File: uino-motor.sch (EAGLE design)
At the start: 26 parts, among them IC1 TB6612FNG, J1 CON_TERMINAL_BLOCK_02-5MM, J2 CON_TERMINAL_BLOCK_02-5MM, J3 CON_TERMINAL_BLOCK_02-5MM, Q1 P-FET, U1 74*1G57, U2 74*1G57

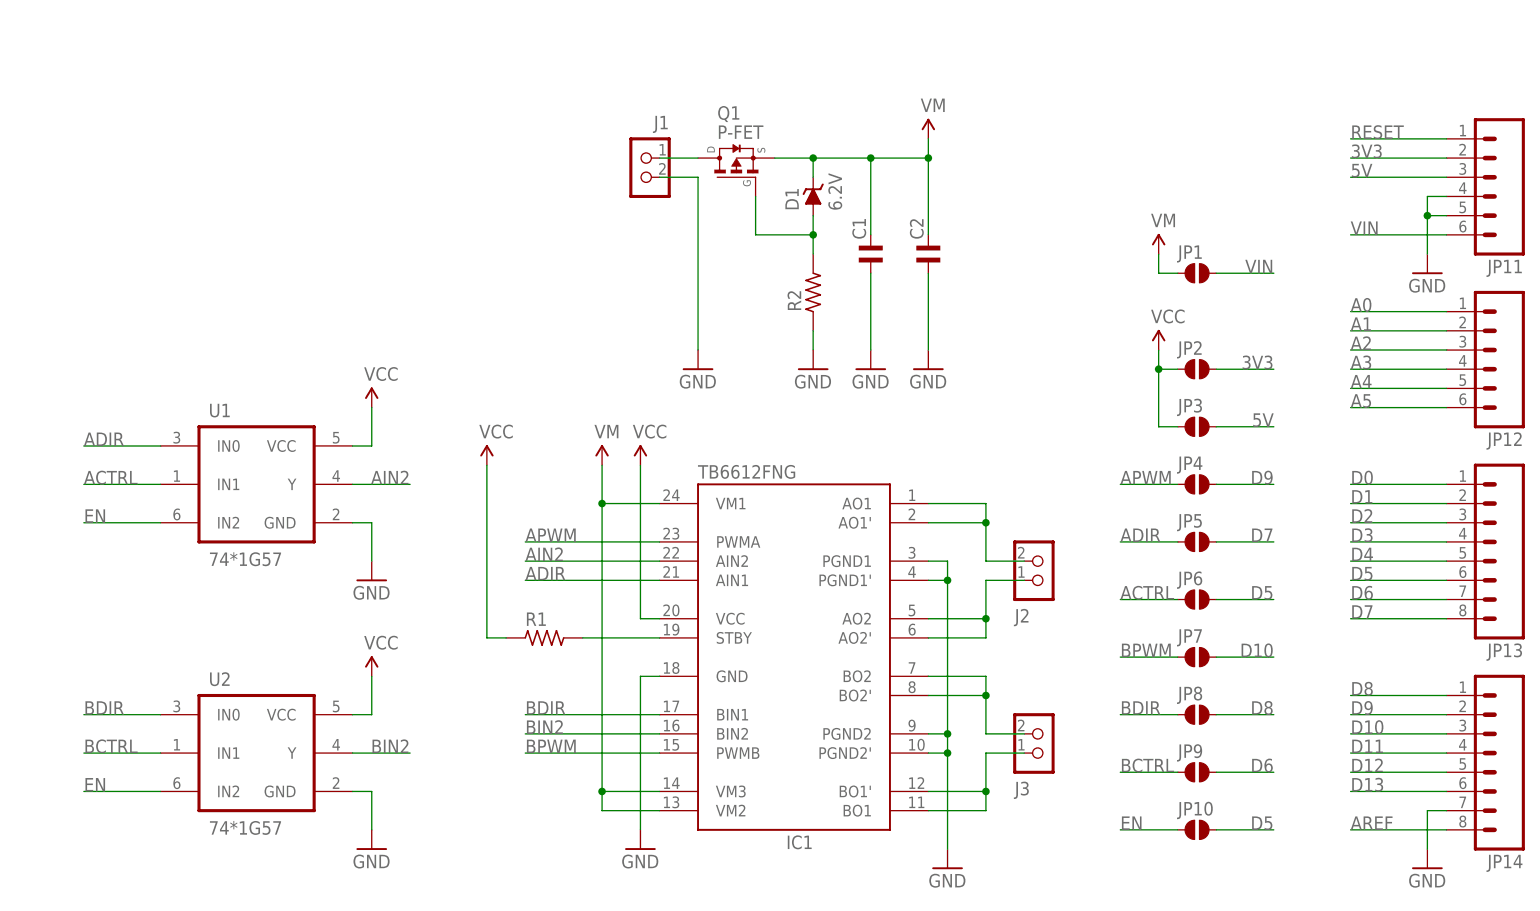
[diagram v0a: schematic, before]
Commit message: Added pull-down at logic gate inputs.  Routed board.
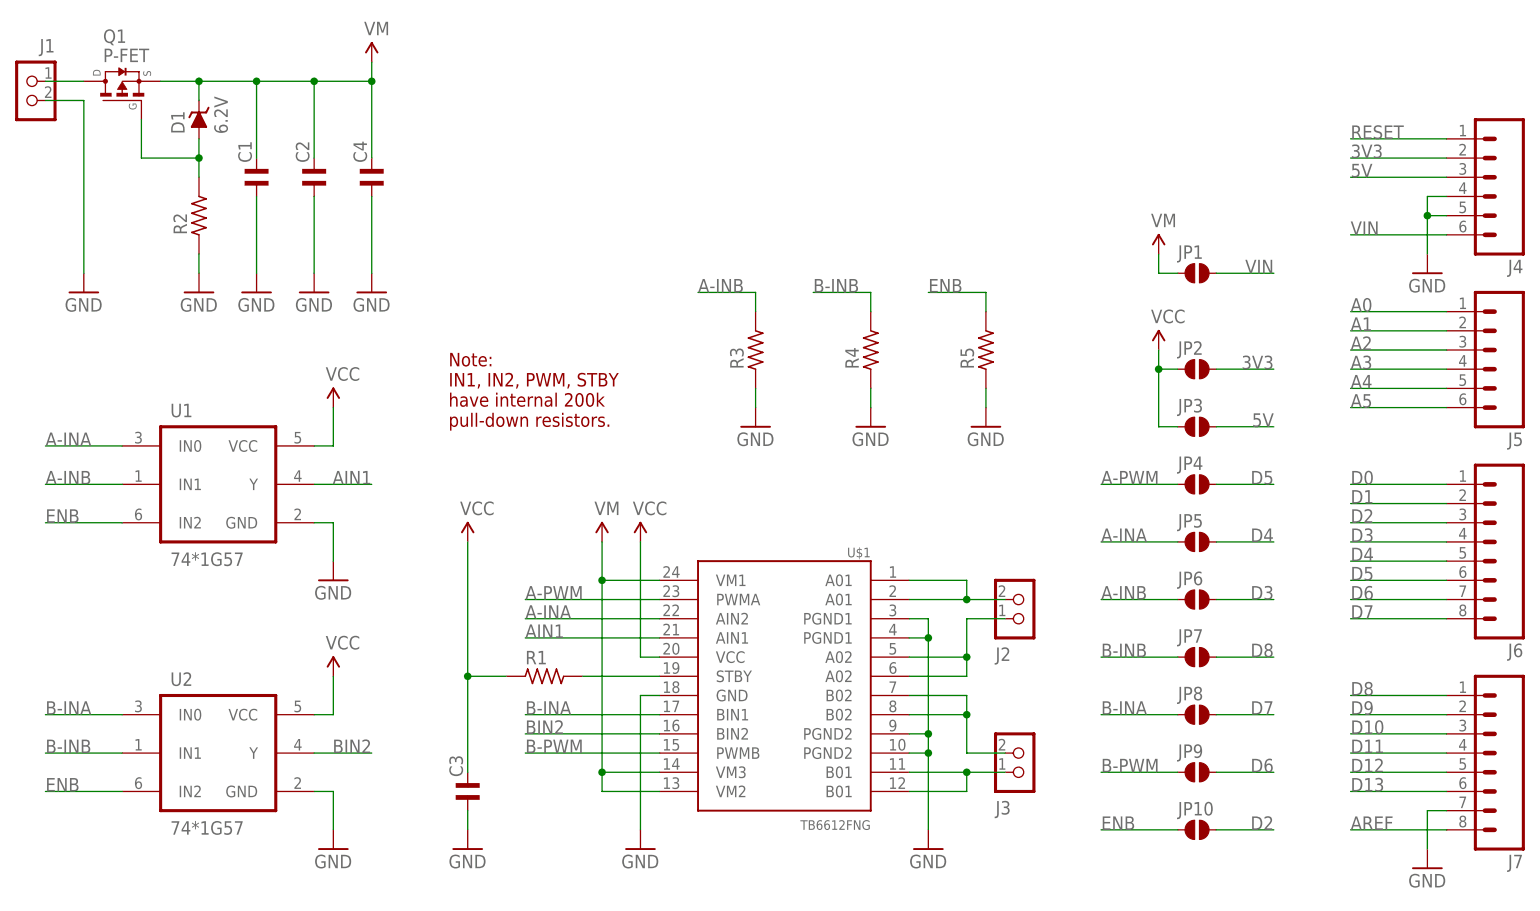
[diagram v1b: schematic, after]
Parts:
- removed IC1: TB6612FNG, adafruit:TB6612FNG
- added C3, C4: (no value), rc-master-smd:C_0805MP
- added R3, R4, R5: (no value), rc-master-smd:R_0805MP
- added U$1: TB6612FNG, SparkFun-PowerIC:TB6612FNG
- JP1, JP10, JP2, JP3, JP4, JP5, JP6, JP7, JP8, JP9: value SJ-055 -> SJ-035; device jumpers:SJ-055 -> jumpers:SJ-035
- renumbered JP11 to J4, JP12 to J5, JP13 to J6, JP14 to J7
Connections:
- removed net ACTRL: JP6.1, U1.IN1
- removed net ADIR: IC1.AIN1, JP5.1, U1.IN0
- removed net AIN2: IC1.AIN2, U1.Y
- removed net APWM: IC1.PWMA, JP4.1
- removed net BCTRL: JP9.1, U2.IN1
- removed net BDIR: IC1.BIN1, JP8.1, U2.IN0
- removed net BPWM: IC1.PWMB, JP7.1
- removed net EN: JP10.1, U1.IN2, U2.IN2
- removed net N$2: IC1.AO2, IC1.AO2', J2.1
- removed net N$3: IC1.BO2, IC1.BO2', J3.2
- removed net N$4: IC1.BO1, IC1.BO1', J3.1
- removed net N$5: IC1.STBY, R1.2
- new net A-INA: JP5.1, U$1.AIN2, U1.IN0
- new net A-INB: JP6.1, R3.2, U1.IN1
- new net A-PWM: JP4.1, U$1.PWMA
- new net AIN1: U$1.AIN1, U1.Y
- new net B-INA: JP8.1, U$1.BIN1, U2.IN0
- new net B-INB: JP7.1, R4.2, U2.IN1
- new net B-PWM: JP9.1, U$1.PWMB
- new net ENB: JP10.1, R5.2, U1.IN2, U2.IN2
- new net N$10: J2.2, U$1.A01@1, U$1.A01@2
- new net N$11: J3.1, U$1.B01@11, U$1.B01@12
- new net N$12: J2.1, U$1.A02@5, U$1.A02@6
- new net N$13: J3.2, U$1.B02@7, U$1.B02@8
- net BIN2: now also U$1.BIN2; no longer IC1.BIN2
- net D10: no longer JP7.2
- net D2: now also JP10.2
- net D3: now also JP6.2
- net D4: now also JP5.2
- net D5: now also JP4.2; no longer JP10.2, JP6.2
- net D7: now also JP8.2; no longer JP5.2
- net D8: now also JP7.2; no longer JP8.2
- net D9: no longer JP4.2
- net GND: now also C3.1, C4.1, R3.1, R4.1, R5.1, U$1.GND, U$1.PGND1@3, U$1.PGND1@4, U$1.PGND2@10, U$1.PGND2@9; no longer IC1.GND, IC1.PGND1, IC1.PGND1', IC1.PGND2, IC1.PGND2'
- net N$1: now also R1.2, U$1.STBY; no longer IC1.AO1, IC1.AO1', J2.2
- net VCC: now also C3.2, U$1.VCC; no longer IC1.VCC
- net VDD: now also C4.2, U$1.VM1, U$1.VM2, U$1.VM3; no longer IC1.VM1, IC1.VM2, IC1.VM3
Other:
- note added: "Note: IN1, IN2, PWM, STBY have internal 200k pull-down resistors."
- moved on the sheet: C1, C2, D1, J1, J2, J3, Q1, R1, R2, U1, U2

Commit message: Parts placed and major routing completed.
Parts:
- added F1: (no value), adi-misc:FUSE_PTC-TH
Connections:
- net N$10 renamed A01
- net N$11 renamed B01
- net N$12 renamed A02
- net N$13 renamed B02
- removed net N$8: J1.1, Q1.D
- new net N$5: F1.1, J1.1
- new net N$7: F1.2, Q1.D
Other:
- moved on the sheet: C1, C2, C4, D1, J1, Q1, R2
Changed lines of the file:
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@@
 <part name="R5" library="rc-master-smd" deviceset="R_" device="0805MP"/>
 <part name="GND15" library="SparkFun-Aesthetics" deviceset="GND" device=""/>
+<part name="F1" library="adi-misc" deviceset="FUSE_PTC" device="-TH"/>
 </parts>
 <sheets>
@@
 <instance part="J2" gate="CON" x="132.08" y="81.28" rot="MR180"/>
 <instance part="J3" gate="CON" x="132.08" y="60.96" rot="MR180"/>
-<instance part="J1" gate="CON" x="5.08" y="152.4" rot="MR0"/>
+<instance part="J1" gate="CON" x="12.7" y="134.62" rot="MR0"/>
 <instance part="GND8" gate="1" x="121.92" y="50.8"/>
 <instance part="GND3" gate="1" x="83.82" y="50.8"/>
@@
 <instance part="R1" gate="G$1" x="71.12" y="73.66"/>
 <instance part="SUPPLY3" gate="G$1" x="60.96" y="91.44"/>
-<instance part="Q1" gate="G$1" x="15.24" y="152.4" smashed="yes" rot="R90">
-<attribute name="VALUE" x="12.7" y="154.94" size="1.778" layer="96"/>
-<attribute name="NAME" x="12.7" y="157.48" size="1.778" layer="95"/>
+<instance part="Q1" gate="G$1" x="25.4" y="152.4" smashed="yes" rot="R90">
+<attribute name="VALUE" x="22.86" y="154.94" size="1.778" layer="96"/>
+<attribute name="NAME" x="22.86" y="157.48" size="1.778" layer="95"/>
 </instance>
-<instance part="D1" gate="G$1" x="25.4" y="147.32" rot="R90"/>
-<instance part="R2" gate="G$1" x="25.4" y="134.62" rot="R90"/>
-<instance part="GND5" gate="1" x="25.4" y="124.46"/>
-<instance part="SUPPLY6" gate="VDD" x="48.26" y="154.94"/>
-<instance part="C1" gate="G$1" x="33.02" y="139.7" rot="R90"/>
-<instance part="C2" gate="G$1" x="40.64" y="139.7" rot="R90"/>
-<instance part="GND6" gate="1" x="33.02" y="124.46"/>
-<instance part="GND7" gate="1" x="40.64" y="124.46"/>
-<instance part="GND4" gate="1" x="10.16" y="124.46"/>
+<instance part="D1" gate="G$1" x="35.56" y="147.32" rot="R90"/>
+<instance part="R2" gate="G$1" x="35.56" y="134.62" rot="R90"/>
+<instance part="GND5" gate="1" x="35.56" y="124.46"/>
+<instance part="SUPPLY6" gate="VDD" x="58.42" y="154.94"/>
+<instance part="C1" gate="G$1" x="43.18" y="139.7" rot="R90"/>
+<instance part="C2" gate="G$1" x="50.8" y="139.7" rot="R90"/>
+<instance part="GND6" gate="1" x="43.18" y="124.46"/>
+<instance part="GND7" gate="1" x="50.8" y="124.46"/>
+<instance part="GND4" gate="1" x="17.78" y="124.46"/>
 <instance part="JP2" gate="G$1" x="157.48" y="114.3"/>
 <instance part="JP3" gate="G$1" x="157.48" y="106.68"/>
@@
 <instance part="GND11" gate="1" x="60.96" y="50.8"/>
 <instance part="U$1" gate="G$1" x="101.6" y="73.66" rot="MR0"/>
-<instance part="C4" gate="G$1" x="48.26" y="139.7" rot="R90"/>
-<instance part="GND12" gate="1" x="48.26" y="124.46"/>
+<instance part="C4" gate="G$1" x="58.42" y="139.7" rot="R90"/>
+<instance part="GND12" gate="1" x="58.42" y="124.46"/>
 <instance part="R3" gate="G$1" x="99.06" y="116.84" rot="R90"/>
 <instance part="GND13" gate="1" x="99.06" y="106.68"/>
@@
 <instance part="R5" gate="G$1" x="129.54" y="116.84" rot="R90"/>
 <instance part="GND15" gate="1" x="129.54" y="106.68"/>
+<instance part="F1" gate="G$1" x="20.32" y="144.78" rot="R90"/>
 </instances>
 <busses>
@@
 <pinref part="C2" gate="G$1" pin="1"/>
 <pinref part="GND7" gate="1" pin="GND"/>
-<wire x1="40.64" y1="137.16" x2="40.64" y2="127" width="0.1524" layer="91"/>
+<wire x1="50.8" y1="137.16" x2="50.8" y2="127" width="0.1524" layer="91"/>
 </segment>
 <segment>
 <pinref part="C1" gate="G$1" pin="1"/>
 <pinref part="GND6" gate="1" pin="GND"/>
-<wire x1="33.02" y1="137.16" x2="33.02" y2="127" width="0.1524" layer="91"/>
-</segment>
-<segment>
-<pinref part="J1" gate="CON" pin="2"/>
-<pinref part="GND4" gate="1" pin="GND"/>
-<wire x1="5.08" y1="149.86" x2="10.16" y2="149.86" width="0.1524" layer="91"/>
-<wire x1="10.16" y1="149.86" x2="10.16" y2="127" width="0.1524" layer="91"/>
+<wire x1="43.18" y1="137.16" x2="43.18" y2="127" width="0.1524" layer="91"/>
 </segment>
 <segment>
 <pinref part="R2" gate="G$1" pin="1"/>
 <pinref part="GND5" gate="1" pin="GND"/>
-<wire x1="25.4" y1="129.54" x2="25.4" y2="127" width="0.1524" layer="91"/>
+<wire x1="35.56" y1="129.54" x2="35.56" y2="127" width="0.1524" layer="91"/>
 </segment>
 <segment>
@@
 <pinref part="C4" gate="G$1" pin="1"/>
 <pinref part="GND12" gate="1" pin="GND"/>
-<wire x1="48.26" y1="137.16" x2="48.26" y2="127" width="0.1524" layer="91"/>
+<wire x1="58.42" y1="137.16" x2="58.42" y2="127" width="0.1524" layer="91"/>
 </segment>
 <segment>
@@
 <pinref part="GND15" gate="1" pin="GND"/>
 <wire x1="129.54" y1="111.76" x2="129.54" y2="109.22" width="0.1524" layer="91"/>
+</segment>
+<segment>
+<pinref part="J1" gate="CON" pin="2"/>
+<pinref part="GND4" gate="1" pin="GND"/>
+<wire x1="12.7" y1="132.08" x2="17.78" y2="132.08" width="0.1524" layer="91"/>
+<wire x1="17.78" y1="132.08" x2="17.78" y2="127" width="0.1524" layer="91"/>
 </segment>
 </net>
@@
 <pinref part="C2" gate="G$1" pin="2"/>
 <pinref part="Q1" gate="G$1" pin="S"/>
-<wire x1="40.64" y1="152.4" x2="40.64" y2="142.24" width="0.1524" layer="91"/>
-<wire x1="20.32" y1="152.4" x2="25.4" y2="152.4" width="0.1524" layer="91"/>
-<junction x="40.64" y="152.4"/>
+<wire x1="50.8" y1="152.4" x2="50.8" y2="142.24" width="0.1524" layer="91"/>
+<wire x1="30.48" y1="152.4" x2="35.56" y2="152.4" width="0.1524" layer="91"/>
+<junction x="50.8" y="152.4"/>
 <pinref part="D1" gate="G$1" pin="C"/>
-<wire x1="25.4" y1="152.4" x2="33.02" y2="152.4" width="0.1524" layer="91"/>
-<wire x1="33.02" y1="152.4" x2="40.64" y2="152.4" width="0.1524" layer="91"/>
-<wire x1="25.4" y1="149.86" x2="25.4" y2="152.4" width="0.1524" layer="91"/>
-<junction x="25.4" y="152.4"/>
+<wire x1="35.56" y1="152.4" x2="43.18" y2="152.4" width="0.1524" layer="91"/>
+<wire x1="43.18" y1="152.4" x2="50.8" y2="152.4" width="0.1524" layer="91"/>
+<wire x1="35.56" y1="149.86" x2="35.56" y2="152.4" width="0.1524" layer="91"/>
+<junction x="35.56" y="152.4"/>
 <pinref part="C1" gate="G$1" pin="2"/>
-<wire x1="33.02" y1="142.24" x2="33.02" y2="152.4" width="0.1524" layer="91"/>
-<junction x="33.02" y="152.4"/>
+<wire x1="43.18" y1="142.24" x2="43.18" y2="152.4" width="0.1524" layer="91"/>
+<junction x="43.18" y="152.4"/>
 <pinref part="C4" gate="G$1" pin="2"/>
-<wire x1="40.64" y1="152.4" x2="48.26" y2="152.4" width="0.1524" layer="91"/>
-<wire x1="48.26" y1="152.4" x2="48.26" y2="142.24" width="0.1524" layer="91"/>
+<wire x1="50.8" y1="152.4" x2="58.42" y2="152.4" width="0.1524" layer="91"/>
+<wire x1="58.42" y1="152.4" x2="58.42" y2="142.24" width="0.1524" layer="91"/>
 <pinref part="SUPPLY6" gate="VDD" pin="VDD"/>
-<wire x1="48.26" y1="154.94" x2="48.26" y2="152.4" width="0.1524" layer="91"/>
-<junction x="48.26" y="152.4"/>
+<wire x1="58.42" y1="154.94" x2="58.42" y2="152.4" width="0.1524" layer="91"/>
+<junction x="58.42" y="152.4"/>
 </segment>
 </net>
@@
 <segment>
 <pinref part="D1" gate="G$1" pin="A"/>
-<wire x1="25.4" y1="144.78" x2="25.4" y2="142.24" width="0.1524" layer="91"/>
+<wire x1="35.56" y1="144.78" x2="35.56" y2="142.24" width="0.1524" layer="91"/>
 <pinref part="Q1" gate="G$1" pin="G"/>
-<wire x1="17.78" y1="147.32" x2="17.78" y2="142.24" width="0.1524" layer="91"/>
-<wire x1="17.78" y1="142.24" x2="25.4" y2="142.24" width="0.1524" layer="91"/>
+<wire x1="27.94" y1="147.32" x2="27.94" y2="142.24" width="0.1524" layer="91"/>
+<wire x1="27.94" y1="142.24" x2="35.56" y2="142.24" width="0.1524" layer="91"/>
 <pinref part="R2" gate="G$1" pin="2"/>
-<wire x1="25.4" y1="139.7" x2="25.4" y2="142.24" width="0.1524" layer="91"/>
-<junction x="25.4" y="142.24"/>
-</segment>
-</net>
-<net name="N$8" class="0">
-<segment>
-<pinref part="J1" gate="CON" pin="1"/>
-<pinref part="Q1" gate="G$1" pin="D"/>
-<wire x1="5.08" y1="152.4" x2="10.16" y2="152.4" width="0.1524" layer="91"/>
+<wire x1="35.56" y1="139.7" x2="35.56" y2="142.24" width="0.1524" layer="91"/>
+<junction x="35.56" y="142.24"/>
 </segment>
 </net>
@@
 </segment>
 </net>
-<net name="N$10" class="0">
+<net name="A01" class="0">
 <segment>
 <pinref part="U$1" gate="G$1" pin="A01@1"/>
@@
 </segment>
 </net>
-<net name="N$11" class="0">
+<net name="B01" class="0">
 <segment>
 <pinref part="U$1" gate="G$1" pin="B01@12"/>
@@
 </segment>
 </net>
-<net name="N$12" class="0">
+<net name="A02" class="0">
 <segment>
 <pinref part="U$1" gate="G$1" pin="A02@6"/>
@@
 </segment>
 </net>
-<net name="N$13" class="0">
+<net name="B02" class="0">
 <segment>
 <pinref part="U$1" gate="G$1" pin="B02@7"/>
@@
 </segment>
 </net>
+<net name="N$5" class="0">
+<segment>
+<pinref part="J1" gate="CON" pin="1"/>
+<pinref part="F1" gate="G$1" pin="1"/>
+<wire x1="12.7" y1="134.62" x2="17.78" y2="134.62" width="0.1524" layer="91"/>
+<wire x1="17.78" y1="134.62" x2="17.78" y2="139.7" width="0.1524" layer="91"/>
+</segment>
+</net>
+<net name="N$7" class="0">
+<segment>
+<pinref part="F1" gate="G$1" pin="2"/>
+<wire x1="17.78" y1="149.86" x2="17.78" y2="152.4" width="0.1524" layer="91"/>
+<pinref part="Q1" gate="G$1" pin="D"/>
+<wire x1="17.78" y1="152.4" x2="20.32" y2="152.4" width="0.1524" layer="91"/>
+</segment>
+</net>

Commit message: Added values. Version 0.1
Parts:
- C1, C2, C3: value (none) -> 10u
- C4: value (none) -> 10y
- R1, R2, R3, R4, R5: value (none) -> 100k
- renumbered U$1 to U3
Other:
- note added: "*uino-motor"
- note added: "by Adi Linden"
- note added: "v0.1 2016/11/12"
